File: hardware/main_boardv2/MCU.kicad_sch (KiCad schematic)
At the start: 32 parts, among them J301 SWD Breakout, U301 W25Q128JVS, U302 RP2040, Y301 ABM8-272-T3

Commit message: dubious hardware schematic 'done'. need to go back and revise passives and verify IC connections, esp the DAC. modified readme
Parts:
- added TP301: XTAL_REF, SamacSys_Parts:bettertestpoint2, symbol Connector:TestPoint
- J301: footprint Connector_PinHeader_2.54mm:PinHeader_1x03_P2.54mm_Vertical -> Connector_PinHeader_2.54mm:PinHeader_1x04_P2.54mm_Vertical
- U302: footprint SC091413 -> SamacSys_Parts:SC091413
- Y301: Mouser Stock/Price (none) -> https://www.mouser.com/ProductDetail/ABRACON/ABM8-272-T3?qs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
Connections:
- net CS_SD: now also U302.28 (GPIO17); no longer U302.32 (GPIO21)
- net ENC1.CLK: now also U302.27 (GPIO16)
- net ENC1.DT: now also U302.18 (GPIO15)
- net ENC1.SW: now also U302.17 (GPIO14)
- net ENC2.CLK: now also U302.31 (GPIO20)
- net ENC2.DT: now also U302.30 (GPIO19)
- net ENC2.SW: now also U302.29 (GPIO18)
- net I2C0.SCL: now also R310.1, U302.7 (GPIO5)
- net I2C0.SDA: now also R309.1, U302.6 (GPIO4)
- net I2C1.SCL: now also R308.1, U302.9 (GPIO7)
- net I2C1.SDA: now also R307.1, U302.8 (GPIO6)
- net LCD_DC: no longer U302.11 (GPIO8)
- net LED_DATA: now also U302.38 (GPIO26_ADC0)
- net RUN_LED1: now also U302.39 (GPIO27_ADC1)
- net RUN_LED2: now also U302.40 (GPIO28_ADC2)
- net I2S0.LRCK: now reaches U302.12 (GPIO9)
- net I2S0.BCK: now reaches U302.13 (GPIO10)
- net DAC.DATA: now reaches U302.14 (GPIO11)
- net DAC.~{MS}: now reaches U302.15 (GPIO12)
- net DAC.MC: now reaches U302.16 (GPIO13)
- net DAC.MD: now reaches U302.34 (GPIO22)
- net UART1.TX: now reaches U302.36 (GPIO24)
- net UART1.RX: now reaches U302.37 (GPIO25)
- net +1V1: no longer names the net of C304.1, C305.1, C306.1, U302.23 (DVDD), U302.45 (VREG_VOUT), U302.50 (DVDD)
- new net I2S0.SCK: U302.11 (GPIO8)
- new net XTAL_REF: TP301.1, U302.32 (GPIO21)
- no-connect marks 0 -> 2
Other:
- note added: "External Flash"
- note added: "internal pullup "should" be fine"
- note added: "referenced MCU design at https://pip-assets.raspberrypi.com/categories/814-rp2040/documents/RP-008279-DS-1-hardware-design-with-rp2040.pdf?disposition=inline"
- note added: "todo: add more GND testpoints across the board"
- note added: "todo: add testpoints or LA breakout for signals!"
- note added: "todo: check if order of this matches pico probe SWD pins"
- note removed: "Flash"
- note removed: "TODO: pull ups on these"
- note removed: "internal pullup "should" do it"
- note removed: "referenced https://pip-assets.raspberrypi.com/categories/814-rp2040/documents/RP-008279-DS-1-hardware-design-with-rp2040.pdf?disposition=inline"

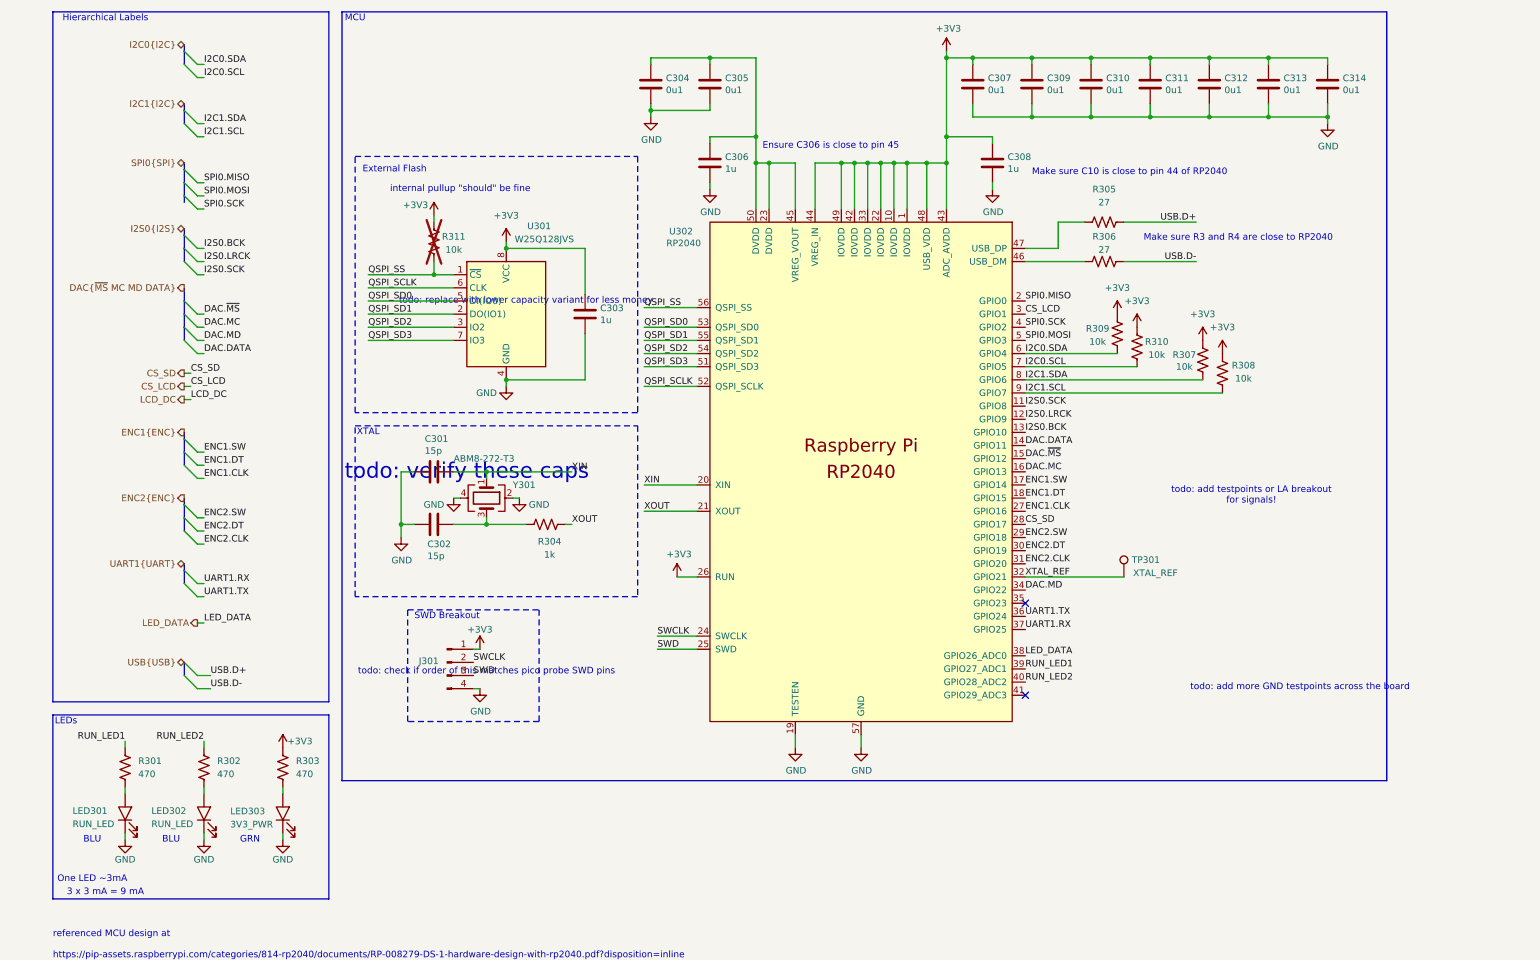
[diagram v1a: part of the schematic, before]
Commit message: schematic sorta done? resized all RC packages to 0805
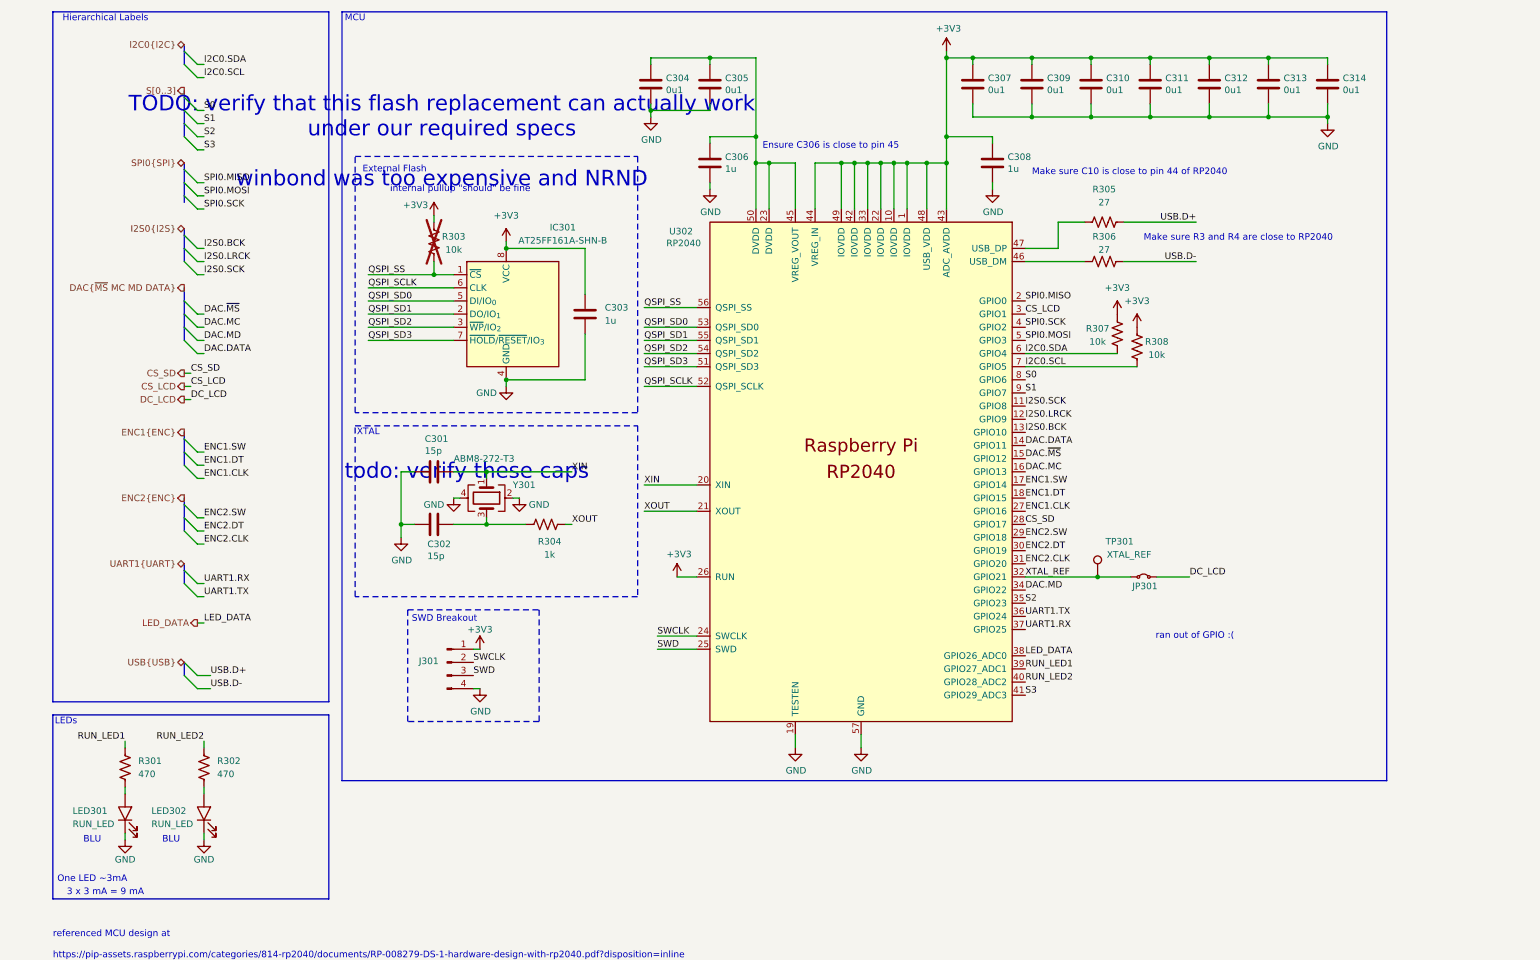
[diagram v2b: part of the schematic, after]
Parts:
- removed C303: 1u, Capacitor_SMD:C_0402_1005Metric, symbol Device:C
- removed LED303: 3V3_PWR, SamacSys_Parts:LEDC2012X40N, symbol ECE445L:LED
- removed R303: 470, Resistor_SMD:R_0805_2012Metric, symbol Device:R_US
- removed R307, R308: 10k, Resistor_SMD:R_0805_2012Metric, symbol Device:R_US
- removed U301: W25Q128JVS, SamacSys_Parts:SOIC127P790X216-8N, symbol Memory_Flash:W25Q128JVS
- added C303: 1u, Capacitor_SMD:C_0805_2012Metric, symbol ECE445L:C
- added IC301: AT25FF161A-SHN-B, SOIC127P798X216-8N, symbol SamacSys_Parts:AT25FF161A-SHN-B
- added JP301: Jumper_2_Small_Bridged, Jumper:SolderJumper-2_P1.3mm_Bridged2Bar_RoundedPad1.0x1.5mm, symbol Jumper:Jumper_2_Small_Bridged
- C301, C302, C304, C305, C306, C307, C308, C309, C310, C311, C312, C313, C314: footprint Capacitor_SMD:C_0402_1005Metric -> Capacitor_SMD:C_0805_2012Metric
- renumbered R311 to R303, R309 to R307, R310 to R308
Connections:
- net +3V3: now also C303.2, IC301.8 (VCC)
- net GND: now also C303.1, IC301.4 (GND)
- net QSPI_SCLK: now also IC301.6 (CLK)
- net QSPI_SD0: now also IC301.5 (DI/IO_{0})
- net QSPI_SD1: now also IC301.2 (DO/IO_{1})
- net QSPI_SD2: now also IC301.3 (~{WP}/IO_{2})
- net QSPI_SD3: now also IC301.7 (~{HOLD}/~{RESET}/IO_{3})
- net QSPI_SS: now also IC301.1 (~{CS})
- net XTAL_REF: now also JP301.1 (A)
- net S2: now reaches U302.35 (GPIO23)
- net S3: now reaches U302.41 (GPIO29_ADC3)
- net I2C1.SCL renamed S1
- net I2C1.SDA renamed S0
- new net DC_LCD: JP301.2 (B)
- no-connect marks 2 -> 0
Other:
- note added: "TODO: verify that this flash replacement can actually work under our required specs winbond was too expensive and NRND"
- note added: "ran out of GPIO :("
- note removed: "GRN"
- note removed: "todo: add more GND testpoints across the board"
- note removed: "todo: add testpoints or LA breakout for signals!"
- note removed: "todo: check if order of this matches pico probe SWD pins"
- note removed: "todo: replace with lower capacity variant for less money"
- moved on the sheet: TP301

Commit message: resized all package to 0603
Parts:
- C301, C302, C304, C305, C306, C307, C308, C309, C310, C311, C312, C313, C314: footprint Capacitor_SMD:C_0805_2012Metric -> Capacitor_SMD:C_0603_1608Metric
- C303: footprint Capacitor_SMD:C_0805_2012Metric -> Capacitor_SMD:C_0603_1608Metric; Mouser Price/Stock https://www.mouser.com/ProductDetail/Samsung-Electro-Mechan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 -> (none)
- R301, R302, R303, R304, R307, R308: footprint Resistor_SMD:R_0805_2012Metric -> Resistor_SMD:R_0603_1608Metric; Mouser Price/Stock https://www.mouser.com/ProductDetail/YAGEO/AF0805JR-07470RL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 -> (none)
- R305, R306: footprint Resistor_SMD:R_0805_2012Metric -> Resistor_SMD:R_0603_1608Metric
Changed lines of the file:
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@@
 			)
 		)
-		(property "Footprint" "Capacitor_SMD:C_0805_2012Metric"
+		(property "Footprint" "Capacitor_SMD:C_0603_1608Metric"
 			(at 192.7352 31.75 0)
 			(effects
@@
 			)
 		)
-		(property "Footprint" "Capacitor_SMD:C_0805_2012Metric"
+		(property "Footprint" "Capacitor_SMD:C_0603_1608Metric"
 			(at 204.1652 31.75 0)
 			(effects
@@
 			)
 		)
-		(property "Footprint" "Capacitor_SMD:C_0805_2012Metric"
+		(property "Footprint" "Capacitor_SMD:C_0603_1608Metric"
 			(at 215.5952 31.75 0)
 			(effects
@@
 			)
 		)
-		(property "Footprint" "Capacitor_SMD:C_0805_2012Metric"
+		(property "Footprint" "Capacitor_SMD:C_0603_1608Metric"
 			(at 227.0252 31.75 0)
 			(effects
@@
 			)
 		)
-		(property "Footprint" "Capacitor_SMD:C_0805_2012Metric"
+		(property "Footprint" "Capacitor_SMD:C_0603_1608Metric"
 			(at 238.4552 31.75 0)
 			(effects
@@
 			)
 		)
-		(property "Footprint" "Capacitor_SMD:C_0805_2012Metric"
+		(property "Footprint" "Capacitor_SMD:C_0603_1608Metric"
 			(at 249.8852 31.75 0)
 			(effects
@@
 			)
 		)
-		(property "Footprint" "Capacitor_SMD:C_0805_2012Metric"
+		(property "Footprint" "Capacitor_SMD:C_0603_1608Metric"
 			(at 261.3152 31.75 0)
 			(effects
@@
 			)
 		)
-		(property "Footprint" "Capacitor_SMD:C_0805_2012Metric"
+		(property "Footprint" "Capacitor_SMD:C_0603_1608Metric"
 			(at 130.5052 31.75 0)
 			(effects
@@
 			)
 		)
-		(property "Footprint" "Capacitor_SMD:C_0805_2012Metric"
+		(property "Footprint" "Capacitor_SMD:C_0603_1608Metric"
 			(at 141.9352 31.75 0)
 			(effects
@@
 			)
 		)
-		(property "Footprint" "Capacitor_SMD:C_0805_2012Metric"
+		(property "Footprint" "Capacitor_SMD:C_0603_1608Metric"
 			(at 141.9352 46.99 0)
 			(effects
@@
 			)
 		)
-		(property "Footprint" "Capacitor_SMD:C_0805_2012Metric"
+		(property "Footprint" "Capacitor_SMD:C_0603_1608Metric"
 			(at 196.5452 46.99 0)
 			(effects
@@
 			)
 		)
-		(property "Footprint" "Capacitor_SMD:C_0805_2012Metric"
+		(property "Footprint" "Capacitor_SMD:C_0603_1608Metric"
 			(at 115.8748 68.58 0)
 			(effects
@@
 			)
 		)
-		(property "Mouser Price/Stock" "https://www.mouser.com/ProductDetail/Samsung-Electro-Mechanics/CL21A106KPFNNNE?qs=sGAEpiMZZMt7gvpyg0xT8jBAVP%252BdkPhuUJvUBe19zr8%3D"
+		(property "Mouser Price/Stock" ""
 			(at 116.84 72.39 0)
 			(effects
@@
 			)
 		)
-		(property "Footprint" "Resistor_SMD:R_0805_2012Metric"
+		(property "Footprint" "Resistor_SMD:R_0603_1608Metric"
 			(at 218.694 75.946 90)
 			(effects
@@
 			)
 		)
-		(property "Mouser Price/Stock" "https://www.mouser.com/ProductDetail/YAGEO/AF0805JR-07470RL?qs=tggtontpCXOaQg0VhtuXeg%3D%3D"
+		(property "Mouser Price/Stock" ""
 			(at 219.71 76.2 0)
 			(effects
@@
 			)
 		)
-		(property "Footprint" "Capacitor_SMD:C_0805_2012Metric"
+		(property "Footprint" "Capacitor_SMD:C_0603_1608Metric"
 			(at 83.82 103.8352 0)
 			(effects
@@
 			)
 		)
-		(property "Footprint" "Resistor_SMD:R_0805_2012Metric"
+		(property "Footprint" "Resistor_SMD:R_0603_1608Metric"
 			(at 86.614 58.166 90)
 			(effects
@@
 			)
 		)
-		(property "Mouser Price/Stock" "https://www.mouser.com/ProductDetail/YAGEO/AF0805JR-07470RL?qs=tggtontpCXOaQg0VhtuXeg%3D%3D"
+		(property "Mouser Price/Stock" ""
 			(at 87.63 58.42 0)
 			(effects
@@
 			)
 		)
-		(property "Footprint" "Resistor_SMD:R_0805_2012Metric"
+		(property "Footprint" "Resistor_SMD:R_0603_1608Metric"
 			(at 222.504 78.486 90)
 			(effects
@@
 			)
 		)
-		(property "Mouser Price/Stock" "https://www.mouser.com/ProductDetail/YAGEO/AF0805JR-07470RL?qs=tggtontpCXOaQg0VhtuXeg%3D%3D"
+		(property "Mouser Price/Stock" ""
 			(at 223.52 78.74 0)
 			(effects
@@
 			)
 		)
-		(property "Footprint" "Resistor_SMD:R_0805_2012Metric"
+		(property "Footprint" "Resistor_SMD:R_0603_1608Metric"
 			(at 217.424 53.594 90)
 			(effects
@@
 			)
 		)
-		(property "Footprint" "Resistor_SMD:R_0805_2012Metric"
+		(property "Footprint" "Resistor_SMD:R_0603_1608Metric"
 			(at 217.424 61.214 90)
 			(effects
@@
 			)
 		)
-		(property "Footprint" "Resistor_SMD:R_0805_2012Metric"
+		(property "Footprint" "Resistor_SMD:R_0603_1608Metric"
 			(at 44.196 160.274 90)
 			(effects
@@
 			)
 		)
-		(property "Mouser Price/Stock" "https://www.mouser.com/ProductDetail/YAGEO/AF0805JR-07470RL?qs=tggtontpCXOaQg0VhtuXeg%3D%3D"
+		(property "Mouser Price/Stock" ""
 			(at 43.18 160.02 0)
 			(effects
@@
 			)
 		)
-		(property "Footprint" "Capacitor_SMD:C_0805_2012Metric"
+		(property "Footprint" "Capacitor_SMD:C_0603_1608Metric"
 			(at 83.82 113.9952 0)
 			(effects
@@
 			)
 		)
-		(property "Footprint" "Resistor_SMD:R_0805_2012Metric"
+		(property "Footprint" "Resistor_SMD:R_0603_1608Metric"
 			(at 28.956 160.274 90)
 			(effects
@@
 			)
 		)
-		(property "Mouser Price/Stock" "https://www.mouser.com/ProductDetail/YAGEO/AF0805JR-07470RL?qs=tggtontpCXOaQg0VhtuXeg%3D%3D"
+		(property "Mouser Price/Stock" ""
 			(at 27.94 160.02 0)
 			(effects
@@
 			)
 		)
-		(property "Footprint" "Resistor_SMD:R_0805_2012Metric"
+		(property "Footprint" "Resistor_SMD:R_0603_1608Metric"
 			(at 109.474 112.014 90)
 			(effects
@@
 			)
 		)
-		(property "Mouser Price/Stock" "https://www.mouser.com/ProductDetail/YAGEO/AF0805JR-07470RL?qs=tggtontpCXOaQg0VhtuXeg%3D%3D"
+		(property "Mouser Price/Stock" ""
 			(at 109.22 113.03 0)
 			(effects
